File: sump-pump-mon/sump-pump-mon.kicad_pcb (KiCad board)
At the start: 2 copper layers, 95.3 x 58.4 mm, 37 parts, among them J1 Main Input, J2 Wall Power, J3 Battery, J4 Display_Conn, J5 Aux Input, J6 I2C, SW3 MODE, SW4 POWER, U1 L7805, U2 4N25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

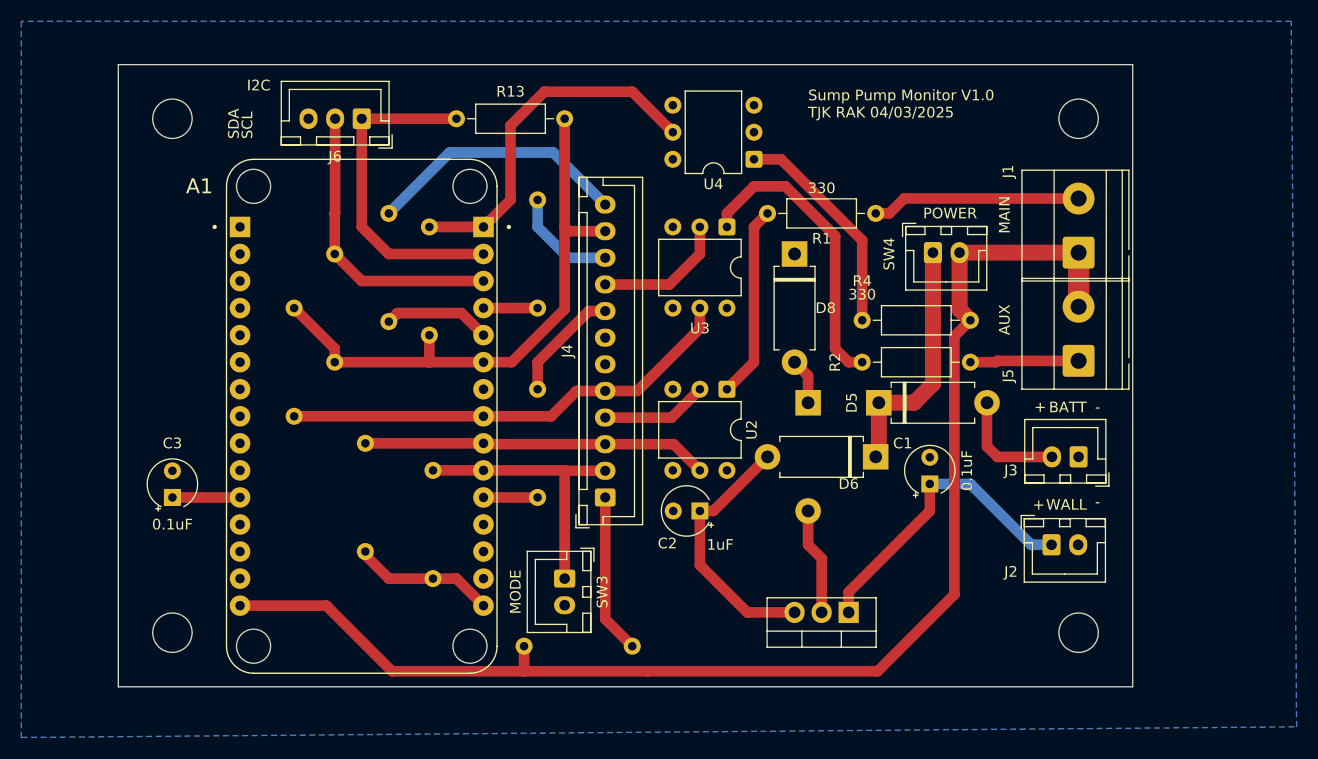
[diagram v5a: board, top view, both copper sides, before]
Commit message: Add Stemma connectors; Add 3d models; Cleanup silk
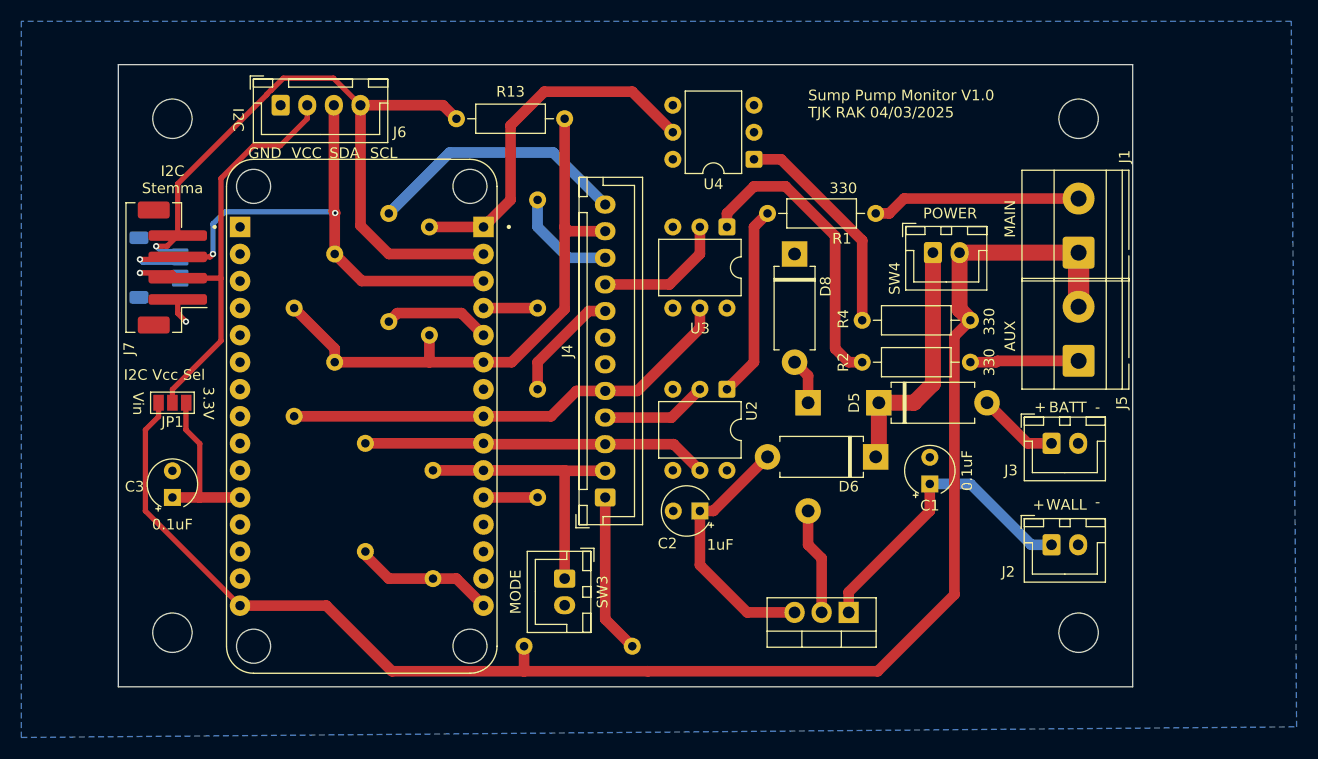
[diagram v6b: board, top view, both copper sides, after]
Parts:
- added J7: I2C Stemma, Connector_JST:JST_PH_B4B-PH-SM4-TB_1x04-1MP_P2.00mm_Vertical, F.Cu at (123.2, 39.4)
- added J8: I2C Stemma QT, Connector_JST:JST_SH_SM04B-SRSS-TB_1x04-1MP_P1.00mm_Horizontal, B.Cu at (121.9, 39.4)
- added JP1: SolderJumper_3_Open, Jumper:SolderJumper-3_P1.3mm_Open_Pad1.0x1.5mm_NumberLabels, F.Cu at (123.2, 52.1)
- J6: footprint Connector_JST:JST_XH_B3B-XH-A_1x03_P2.50mm_Vertical -> Connector_JST:JST_XH_B4B-XH-A_1x04_P2.50mm_Vertical
- moved J6 7.73 mm to (133.3, 24.1), turned to 0 degrees
- moved J3 2.84 mm to (205.7, 55.9), turned to 0 degrees
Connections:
- J3 pad 1: GND -> Net-(D5-A)
- J3 pad 2: Net-(D5-A) -> GND
- J6 pad 1: Net-(A1B-D1) -> GND
- J6 pad 2: Net-(A1B-D2) -> Net-(J6-Pin_2)
- J6 pad 3: GND -> Net-(A1B-D2)
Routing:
- net Net-(J6-Pin_2): track 0.00 -> 46.2 mm, vias 0 -> 1
- net Net-(A1B-D1): track 31.5 -> 65.6 mm, vias 0 -> 1
- net Net-(A1B-D2): track 27.7 -> 55.0 mm, vias 0 -> 3
- net Vin: track 124.4 -> 147.6 mm
- net +3.3V: track 74.5 -> 83.9 mm
- net Net-(D5-A): track 10.6 -> 7.64 mm
- net GND: track 0.00 -> 2.40 mm, vias 0 -> 1
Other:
- board text added: "3.3V"
- board text added: "GND"
- board text added: "I2C Stemma"
- board text added: "I2C Stemma QT"
- board text added: "I2C Vcc Sel"
- board text added: "VCC"
- board text added: "Vin"

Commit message: Enter OSHPark design rules; thicken silk to meet requirement
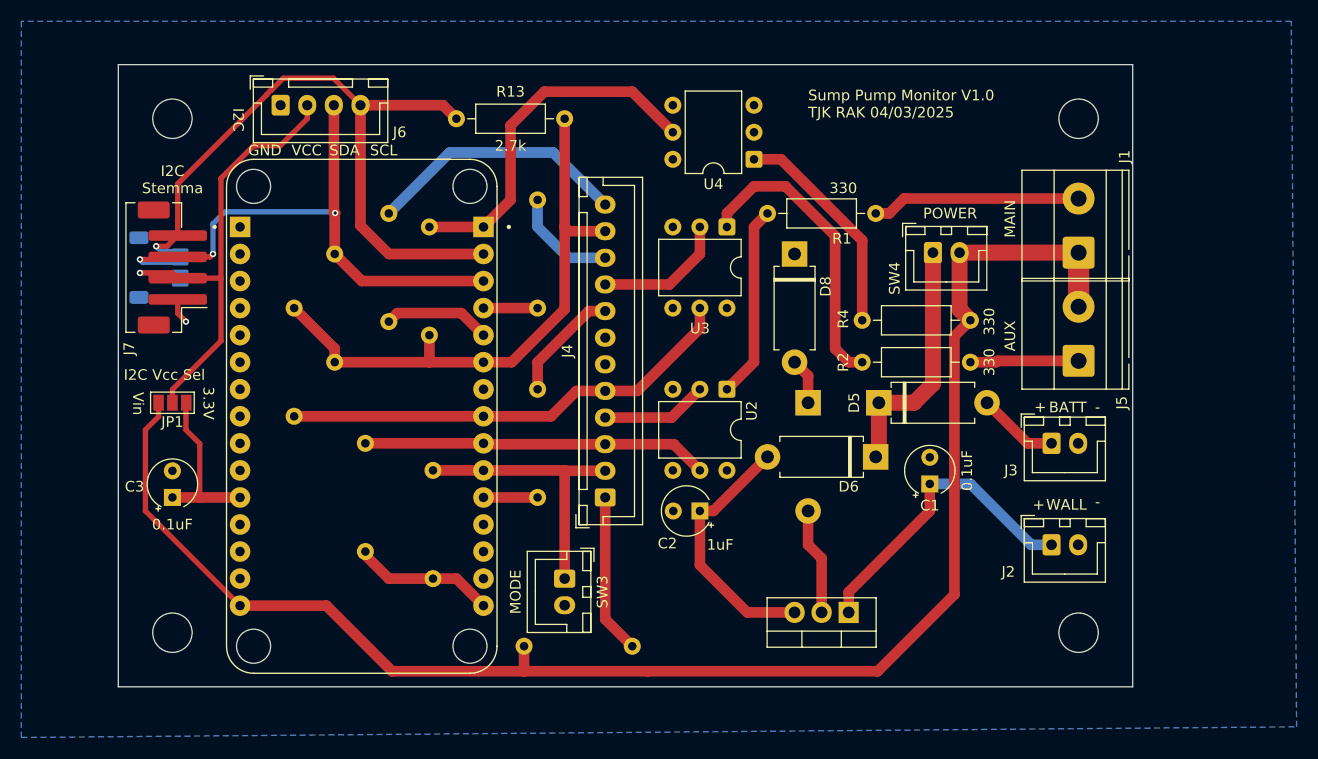
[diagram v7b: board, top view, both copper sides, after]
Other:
- rule pad_to_mask_clearance: 0 -> 0.0508
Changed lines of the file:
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@@
 	)
 	(setup
-		(pad_to_mask_clearance 0)
+		(pad_to_mask_clearance 0.0508)
 		(allow_soldermask_bridges_in_footprints no)
 		(tenting front back)
@@
 		(property "Value" "2.7k"
 			(at 5.08 -2.54 0)
-			(layer "F.Fab")
+			(layer "F.SilkS")
 			(effects
 				(font
@@
 			(font
 				(size 1 1)
-				(thickness 0.1)
+				(thickness 0.15)
 			)
 			(justify left bottom)
@@
 	)
 	(gr_text "VCC"
-		(at 134.366 29.21 0)
+		(at 134.366 28.956 0)
 		(layer "F.SilkS")
 		(effects
 			(font
 				(size 1 1)
-				(thickness 0.1)
+				(thickness 0.15)
 			)
 			(justify left bottom)
@@
 			(font
 				(size 1 1)
-				(thickness 0.125)
+				(thickness 0.15)
 			)
 			(justify left bottom)
@@
 			(font
 				(size 1 1)
-				(thickness 0.1)
+				(thickness 0.15)
 			)
 			(justify left bottom)
@@
 			(font
 				(size 1 1)
-				(thickness 0.1)
+				(thickness 0.15)
 			)
 			(justify left bottom)
@@
 			(font
 				(size 1 1)
-				(thickness 0.125)
+				(thickness 0.15)
 			)
 			(justify left bottom)
@@
 			(font
 				(size 1 1)
-				(thickness 0.1)
+				(thickness 0.15)
 			)
 			(justify left bottom)
@@
 			(font
 				(size 1 1)
-				(thickness 0.1)
+				(thickness 0.15)
 			)
 			(justify left bottom)
@@
 			(font
 				(size 1 1)
-				(thickness 0.1)
+				(thickness 0.15)
 			)
 			(justify left bottom)
@@
 			(font
 				(size 1 1)
-				(thickness 0.1)
+				(thickness 0.15)
 			)
 			(justify left bottom)
@@
 	)
 	(gr_text "GND"
-		(at 130.302 29.21 0)
+		(at 130.302 28.956 0)
 		(layer "F.SilkS")
 		(effects
 			(font
 				(size 1 1)
-				(thickness 0.1)
+				(thickness 0.15)
 			)
 			(justify left bottom)
@@
 	)
 	(gr_text "SDA"
-		(at 137.922 29.21 0)
+		(at 137.922 28.956 0)
 		(layer "F.SilkS")
 		(effects
 			(font
 				(size 1 1)
-				(thickness 0.1)
+				(thickness 0.15)
 			)
 			(justify left bottom)
@@
 	)
 	(gr_text "SCL"
-		(at 141.732 29.21 0)
+		(at 141.732 28.956 0)
 		(layer "F.SilkS")
 		(effects
 			(font
 				(size 1 1)
-				(thickness 0.1)
+				(thickness 0.15)
 			)
 			(justify left bottom)
@@
 			(font
 				(size 1 1)
-				(thickness 0.1)
+				(thickness 0.15)
 			)
 			(justify left bottom)
@@
 			(font
 				(size 1 1)
-				(thickness 0.1)
+				(thickness 0.15)
 			)
 			(justify left bottom)
@@
 			(font
 				(size 1 1)
-				(thickness 0.1)
+				(thickness 0.15)
 			)
 			(justify left bottom)
@@
 			(font
 				(size 1 1)
-				(thickness 0.1)
+				(thickness 0.15)
 			)
 			(justify left bottom)
@@
 			(font
 				(size 1 1)
-				(thickness 0.125)
+				(thickness 0.15)
 			)
 			(justify bottom)
@@
 			(font
 				(size 1 1)
-				(thickness 0.125)
+				(thickness 0.15)
 			)
 			(justify bottom mirror)
